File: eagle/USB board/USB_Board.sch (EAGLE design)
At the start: 13 parts, among them U2 FT232RLSSOP

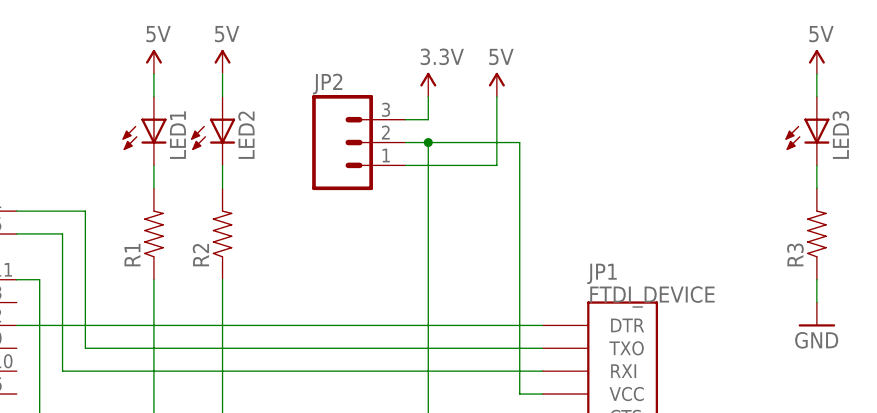
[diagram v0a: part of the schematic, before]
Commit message: First version of USB Board
Oops, forgot to put in drill holes.
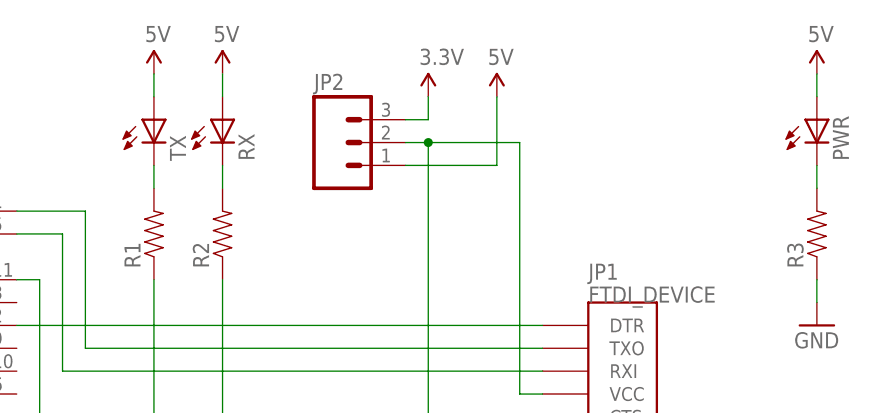
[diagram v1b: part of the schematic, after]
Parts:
- renumbered LED1 to TX, LED2 to RX, LED3 to PWR
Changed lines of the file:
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@@
 <part name="R1" library="SparkFun-Resistors" deviceset="10KOHM1/6W5%(PTH)" device="KIT"/>
 <part name="R2" library="SparkFun-Resistors" deviceset="10KOHM1/6W5%(PTH)" device="KIT"/>
-<part name="LED1" library="SparkFun-LED" deviceset="LED" device="5MM"/>
-<part name="LED2" library="SparkFun-LED" deviceset="LED" device="5MM"/>
+<part name="TX" library="SparkFun-LED" deviceset="LED" device="5MM"/>
+<part name="RX" library="SparkFun-LED" deviceset="LED" device="5MM"/>
 <part name="SUPPLY5" library="SparkFun-Aesthetics" deviceset="5V" device=""/>
 <part name="SUPPLY6" library="SparkFun-Aesthetics" deviceset="5V" device=""/>
 <part name="R3" library="SparkFun-Resistors" deviceset="10KOHM1/6W5%(PTH)" device="KIT"/>
-<part name="LED3" library="SparkFun-LED" deviceset="LED" device="5MM"/>
+<part name="PWR" library="SparkFun-LED" deviceset="LED" device="5MM"/>
 <part name="SUPPLY7" library="SparkFun-Aesthetics" deviceset="5V" device=""/>
 <part name="GND6" library="SparkFun-Aesthetics" deviceset="GND" device=""/>
@@
 <instance part="R1" gate="G$1" x="124.46" y="127" rot="R90"/>
 <instance part="R2" gate="G$1" x="132.08" y="127" rot="R90"/>
-<instance part="LED1" gate="G$1" x="124.46" y="139.7"/>
-<instance part="LED2" gate="G$1" x="132.08" y="139.7"/>
+<instance part="TX" gate="G$1" x="124.46" y="139.7"/>
+<instance part="RX" gate="G$1" x="132.08" y="139.7"/>
 <instance part="SUPPLY5" gate="G$1" x="124.46" y="144.78"/>
 <instance part="SUPPLY6" gate="G$1" x="132.08" y="144.78"/>
 <instance part="R3" gate="G$1" x="198.12" y="127" rot="R90"/>
-<instance part="LED3" gate="G$1" x="198.12" y="139.7"/>
+<instance part="PWR" gate="G$1" x="198.12" y="139.7"/>
 <instance part="SUPPLY7" gate="G$1" x="198.12" y="144.78"/>
 <instance part="GND6" gate="1" x="198.12" y="116.84"/>
@@
 </segment>
 <segment>
-<pinref part="LED1" gate="G$1" pin="A"/>
+<pinref part="TX" gate="G$1" pin="A"/>
 <pinref part="SUPPLY5" gate="G$1" pin="5V"/>
 <wire x1="124.46" y1="142.24" x2="124.46" y2="144.78" width="0.1524" layer="91"/>
 </segment>
 <segment>
-<pinref part="LED2" gate="G$1" pin="A"/>
+<pinref part="RX" gate="G$1" pin="A"/>
 <pinref part="SUPPLY6" gate="G$1" pin="5V"/>
 <wire x1="132.08" y1="142.24" x2="132.08" y2="144.78" width="0.1524" layer="91"/>
 </segment>
 <segment>
-<pinref part="LED3" gate="G$1" pin="A"/>
+<pinref part="PWR" gate="G$1" pin="A"/>
 <pinref part="SUPPLY7" gate="G$1" pin="5V"/>
 <wire x1="198.12" y1="142.24" x2="198.12" y2="144.78" width="0.1524" layer="91"/>
@@
 <net name="N$15" class="0">
 <segment>
-<pinref part="LED1" gate="G$1" pin="C"/>
+<pinref part="TX" gate="G$1" pin="C"/>
 <pinref part="R1" gate="G$1" pin="2"/>
 <wire x1="124.46" y1="134.62" x2="124.46" y2="132.08" width="0.1524" layer="91"/>
@@
 <net name="N$16" class="0">
 <segment>
-<pinref part="LED2" gate="G$1" pin="C"/>
+<pinref part="RX" gate="G$1" pin="C"/>
 <pinref part="R2" gate="G$1" pin="2"/>
 <wire x1="132.08" y1="134.62" x2="132.08" y2="132.08" width="0.1524" layer="91"/>
@@
 <net name="N$17" class="0">
 <segment>
-<pinref part="LED3" gate="G$1" pin="C"/>
+<pinref part="PWR" gate="G$1" pin="C"/>
 <pinref part="R3" gate="G$1" pin="2"/>
 <wire x1="198.12" y1="134.62" x2="198.12" y2="132.08" width="0.1524" layer="91"/>
@@
 </sheet>
 </sheets>
+<errors>
+</errors>
 </schematic>
 </drawing>
